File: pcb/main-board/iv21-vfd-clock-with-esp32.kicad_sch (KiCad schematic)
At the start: 24 parts, among them J1 Conn_02x10_Odd_Even, J2 4328, P1 USB_C_Plug_USB2.0, SW1 SW_SPST, SW2 SW_SPST, U1 MAX6921AQI_, U2 MOUDLE-SEEEDUINO-XIAO-ESP32C3, U3 AP3012, U4 S-1167B24

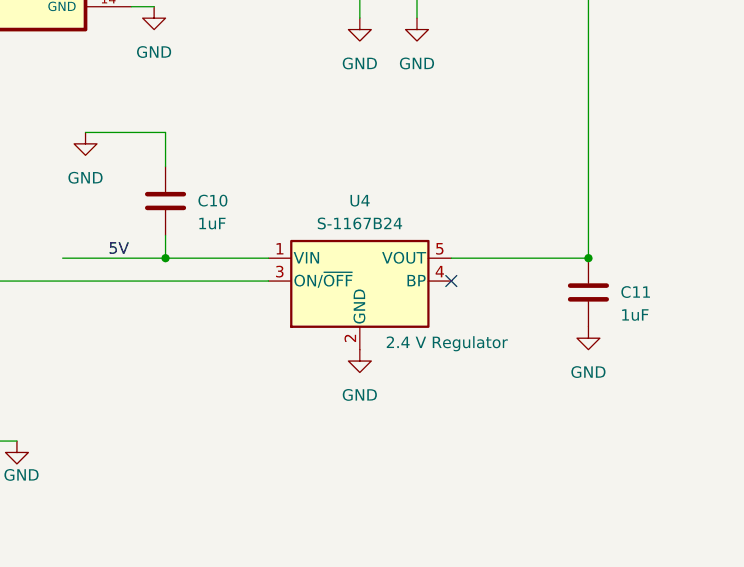
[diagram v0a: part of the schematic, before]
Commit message: Add voltage regulator schematic symbol from dad.
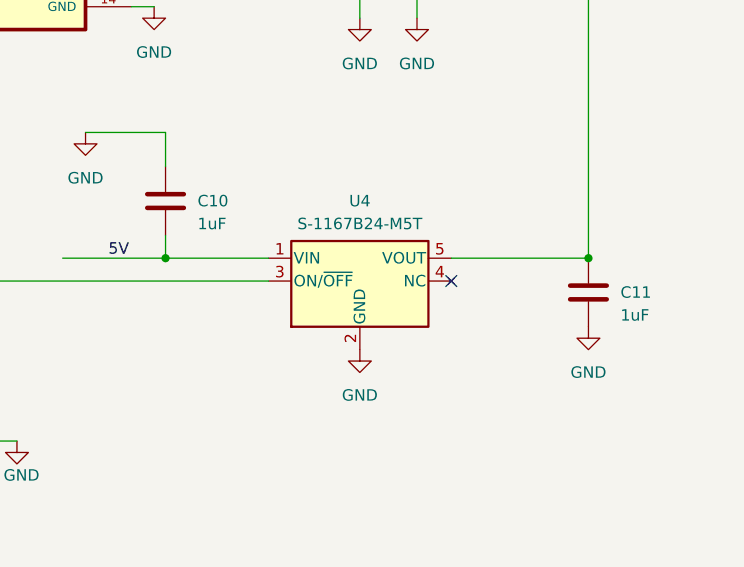
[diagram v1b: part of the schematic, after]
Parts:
- removed U4: S-1167B24, Package_TO_SOT_SMD:SOT-23-5, symbol Regulator_Linear:LP2985-1.8
- added U4: S-1167B24-M5T, Package_TO_SOT_SMD:SOT-23-5, symbol S-1167B24-M5T:LP2985-3.0
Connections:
- net 5V: now also U4.1 (VIN)
- net GND: now also U4.2 (GND)
- net at C11.1, J1.18 (Pin_18): now also U4.5 (VOUT)
- net at U2.3 (PA10_A2_D2): now also U4.3 (ON/~{OFF})
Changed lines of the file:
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@@
-	)
-	(symbol
-		(lib_id "Regulator_Linear:LP2985-1.8")
-		(at 203.2 135.89 0)
-		(unit 1)
-		(exclude_from_sim no)
-		(in_bom yes)
-		(on_board yes)
-		(dnp no)
-		(property "Reference" "U4"
-			(at 203.2 127 0)
-			(effects
-				(font
-					(size 1.27 1.27)
-				)
-			)
-		)
-		(property "Value" "S-1167B24"
-			(at 203.2 129.54 0)
-			(effects
-				(font
-					(size 1.27 1.27)
-				)
-			)
-		)
-		(property "Footprint" "Package_TO_SOT_SMD:SOT-23-5"
-			(at 203.2 127.635 0)
-			(effects
-				(font
-					(size 1.27 1.27)
-				)
-				(hide yes)
-			)
-		)
-		(property "Datasheet" "https://www.mouser.com/datasheet/2/1490/S1167_E-3431012.pdf"
-			(at 203.2 135.89 0)
-			(effects
-				(font
-					(size 1.27 1.27)
-				)
-				(hide yes)
-			)
-		)
-		(property "Description" "S-1167B24-M5T1U: LDO Voltage Regulators ULTRA LOW CURRENT CONSUMPTION, HIGH RIPPLE REJECTION AND LOW DROPOUT CMOS VOLTAGE REGULATOR"
-			(at 203.2 135.89 0)
-			(effects
-				(font
-					(size 1.27 1.27)
-				)
-				(hide yes)
-			)
-		)
-		(property "URL" "https://www.mouser.com/ProductDetail/ABLIC/S-1167B24-M5T1U?qs=2wMNvWM5ZX5qdX7pUf9HBw%3D%3D"
-			(at 203.2 135.89 0)
-			(effects
-				(font
-					(size 1.27 1.27)
-				)
-				(hide yes)
-			)
-		)
-		(property "Label" "2.4 V Regulator"
-			(at 212.852 142.748 0)
-			(effects
-				(font
-					(size 1.27 1.27)
-				)
-			)
-		)
-		(pin "4"
-		)
-		(pin "1"
-		)
-		(pin "3"
-		)
-		(pin "2"
-		)
-		(pin "5"
-		)
-		(instances
-			(project ""
-				(path "/f4ccf12f-2c39-4319-adc8-75ef731d1807"
-					(reference "U4")
-					(unit 1)
-				)
-			)
-		)
 	)
 	(symbol
@@
 					(unit 1)
 				)
+			)
+		)
+	)
+	(symbol
+		(lib_id "S-1167B24-M5T:LP2985-3.0")
+		(at 203.2 135.89 0)
+		(unit 1)
+		(exclude_from_sim no)
+		(in_bom yes)
+		(on_board yes)
+		(dnp no)
+		(fields_autoplaced yes)
+		(property "Reference" "U4"
+			(at 203.2 127 0)
+			(effects
+				(font
+					(size 1.27 1.27)
+				)
+			)
+		)
+		(property "Value" "S-1167B24-M5T"
+			(at 203.2 129.54 0)
+			(effects
+				(font
+					(size 1.27 1.27)
+				)
+			)
+		)
+		(property "Footprint" "Package_TO_SOT_SMD:SOT-23-5"
+			(at 203.2 127.635 0)
+			(effects
+				(font
+					(size 1.27 1.27)
+				)
+				(hide yes)
+			)
+		)
+		(property "Datasheet" "http://www.ti.com/lit/ds/symlink/lp2985.pdf"
+			(at 203.2 135.89 0)
+			(effects
+				(font
+					(size 1.27 1.27)
+				)
+				(hide yes)
+			)
+		)
+		(property "Description" "150mA 16V Low-noise Low-dropout Regulator With Shutdown, 3.0V output voltage, SOT-23-5"
+			(at 203.2 135.89 0)
+			(effects
+				(font
+					(size 1.27 1.27)
+				)
+				(hide yes)
+			)
+		)
+		(pin "1"
+		)
+		(pin "4"
+		)
+		(pin "2"
+		)
+		(pin "3"
+		)
+		(pin "5"
+		)
+		(instances
+			(project ""
+				(path "/f4ccf12f-2c39-4319-adc8-75ef731d1807"
+					(reference "U4")
+					(unit 1)
+				)

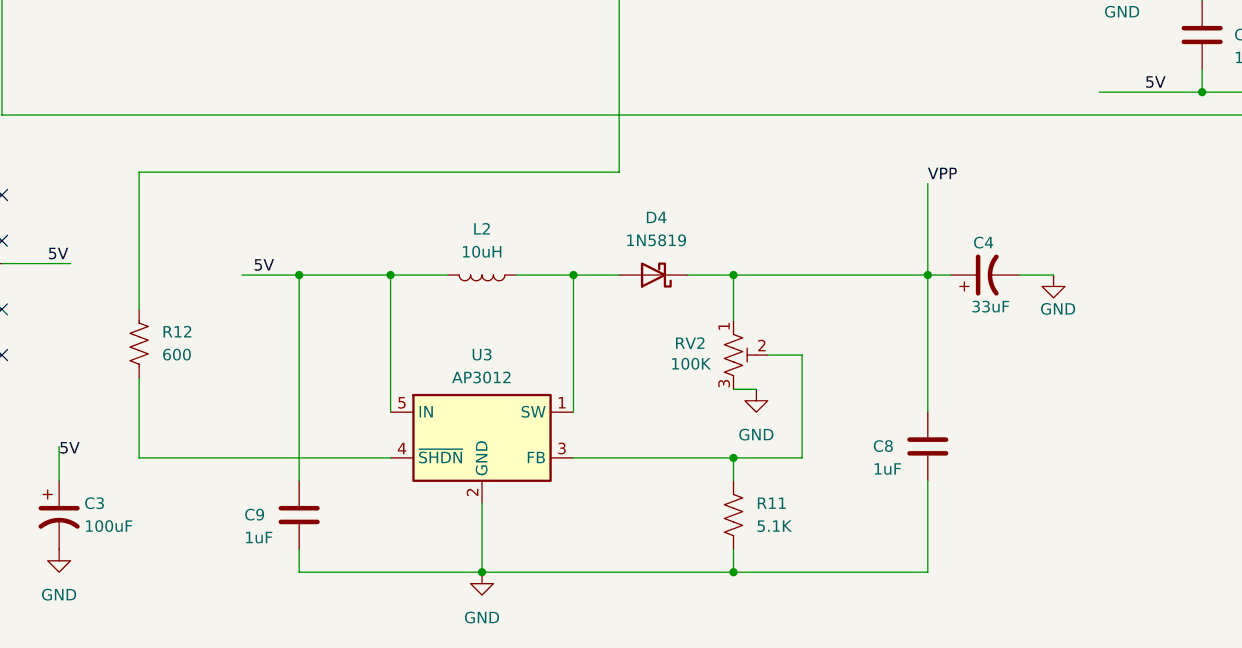
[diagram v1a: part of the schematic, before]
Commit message: Schematic updates for VPP.
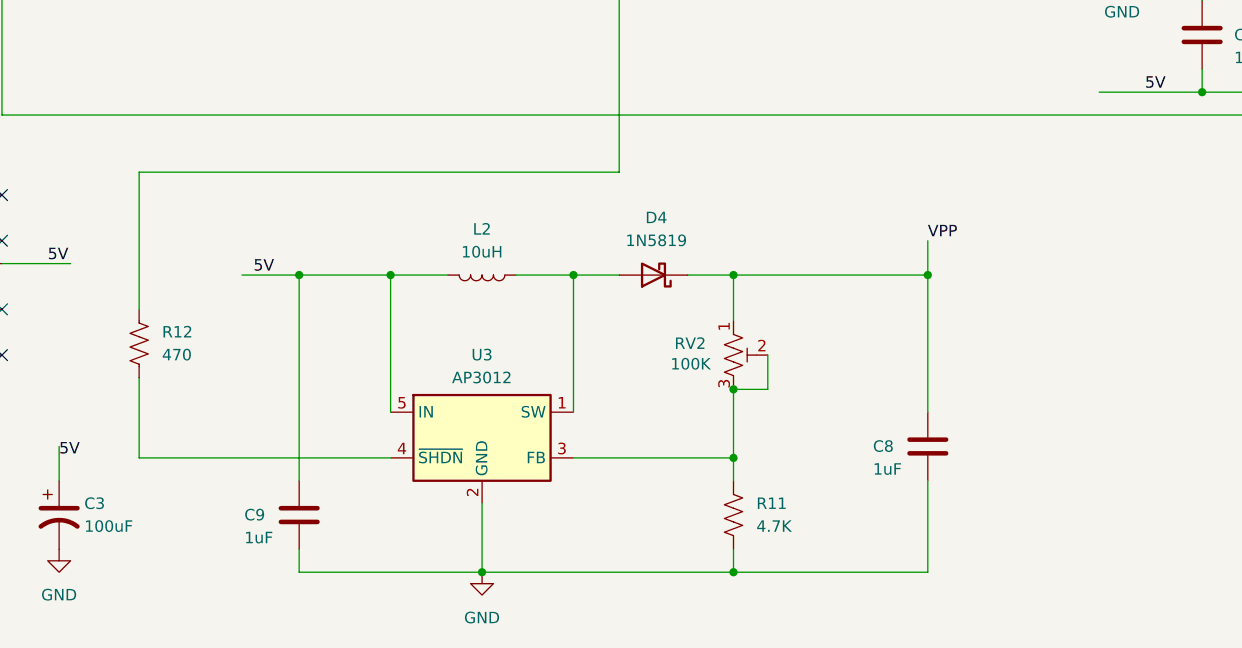
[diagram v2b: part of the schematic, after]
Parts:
- removed C4: 33uF, Capacitor_SMD:CP_Elec_8x10.5, symbol Device:C_Polarized_US
- R11: value 5.1K -> 4.7K
- R12: value 600 -> 470
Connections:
- net GND: no longer RV2.3
- net at R11.1, RV2.2, U3.3 (FB): now also RV2.3

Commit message: - Widen width of power traces. (Need to reroute one of the voltage regulators, still) - Update voltage regulator datasheet and product URL.
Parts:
- U4: Product URL (none) -> https://www.mouser.com/ProductDetail/628-S-1167B24-M5T1U
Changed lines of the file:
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@@
 			)
 		)
-		(property "Datasheet" "http://www.ti.com/lit/ds/symlink/lp2985.pdf"
+		(property "Datasheet" "https://www.mouser.com/datasheet/2/1490/S1167_E-3431012.pdf"
 			(at 203.2 135.89 0)
 			(effects
@@
 			(at 203.2 135.89 0)
 			(effects
+				(font
+					(size 1.27 1.27)
+				)
+				(hide yes)
+			)
+		)
+		(property "Product URL" "https://www.mouser.com/ProductDetail/628-S-1167B24-M5T1U"
+			(at 203.2 135.89 0)
+			(effects

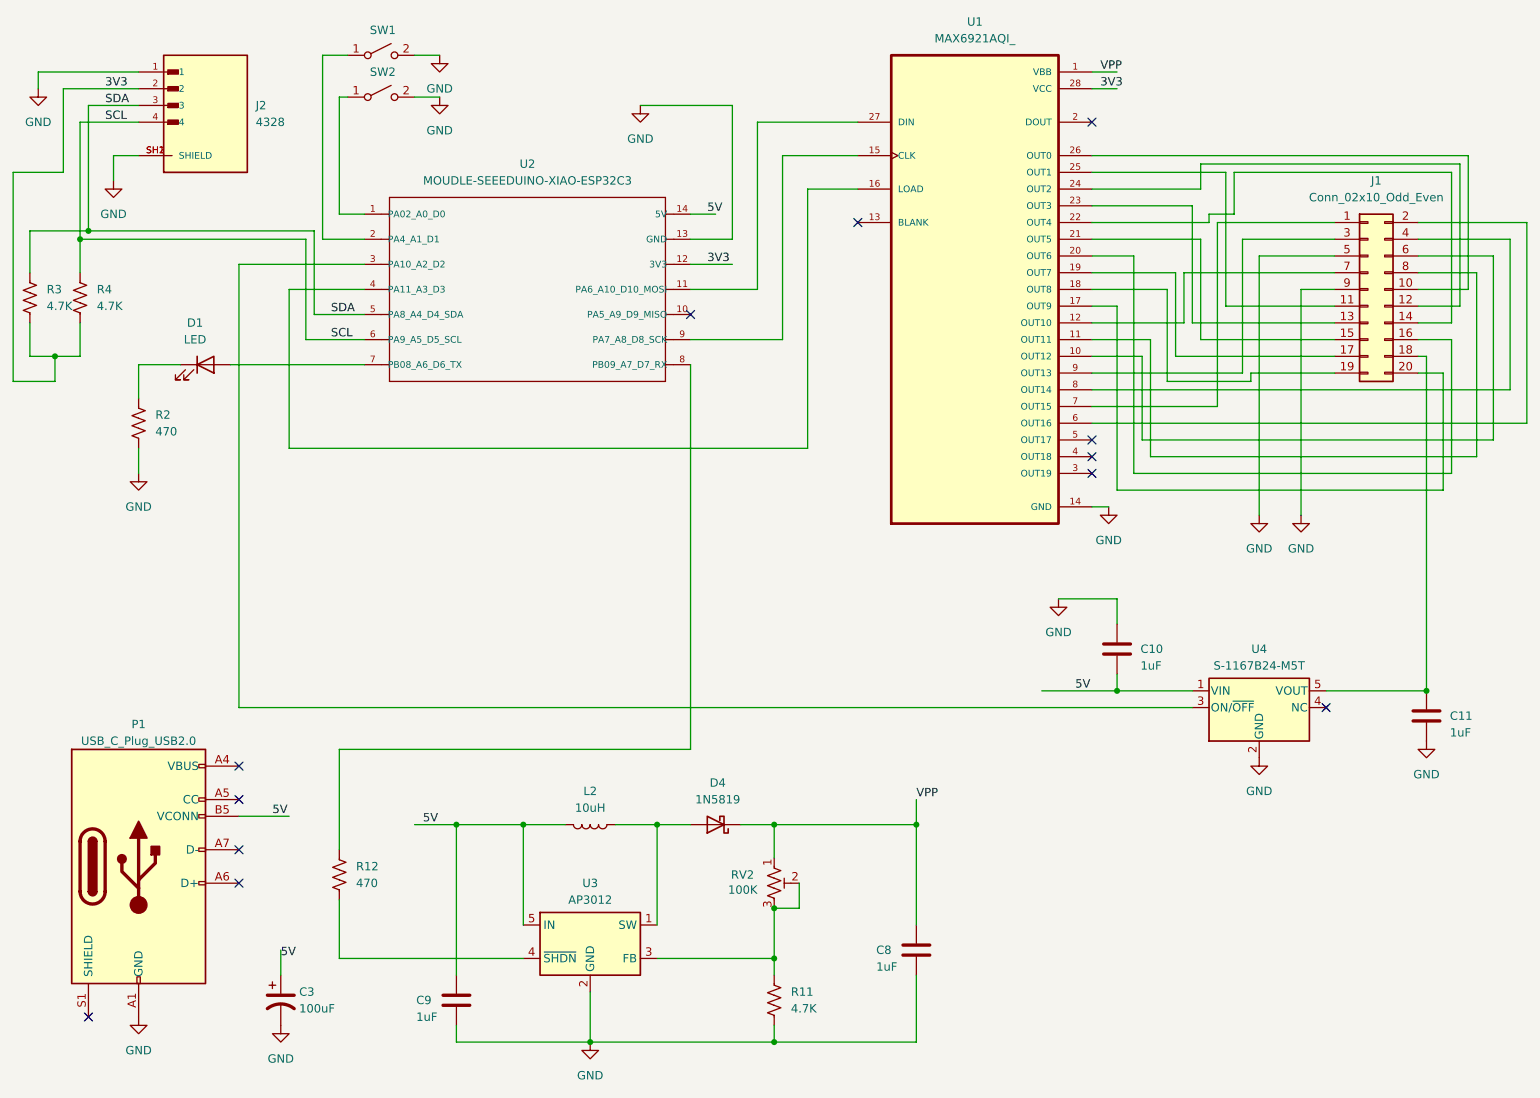
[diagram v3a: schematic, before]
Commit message: - Update power traces - Add in-series resistor with VPP voltage divider trim pot.
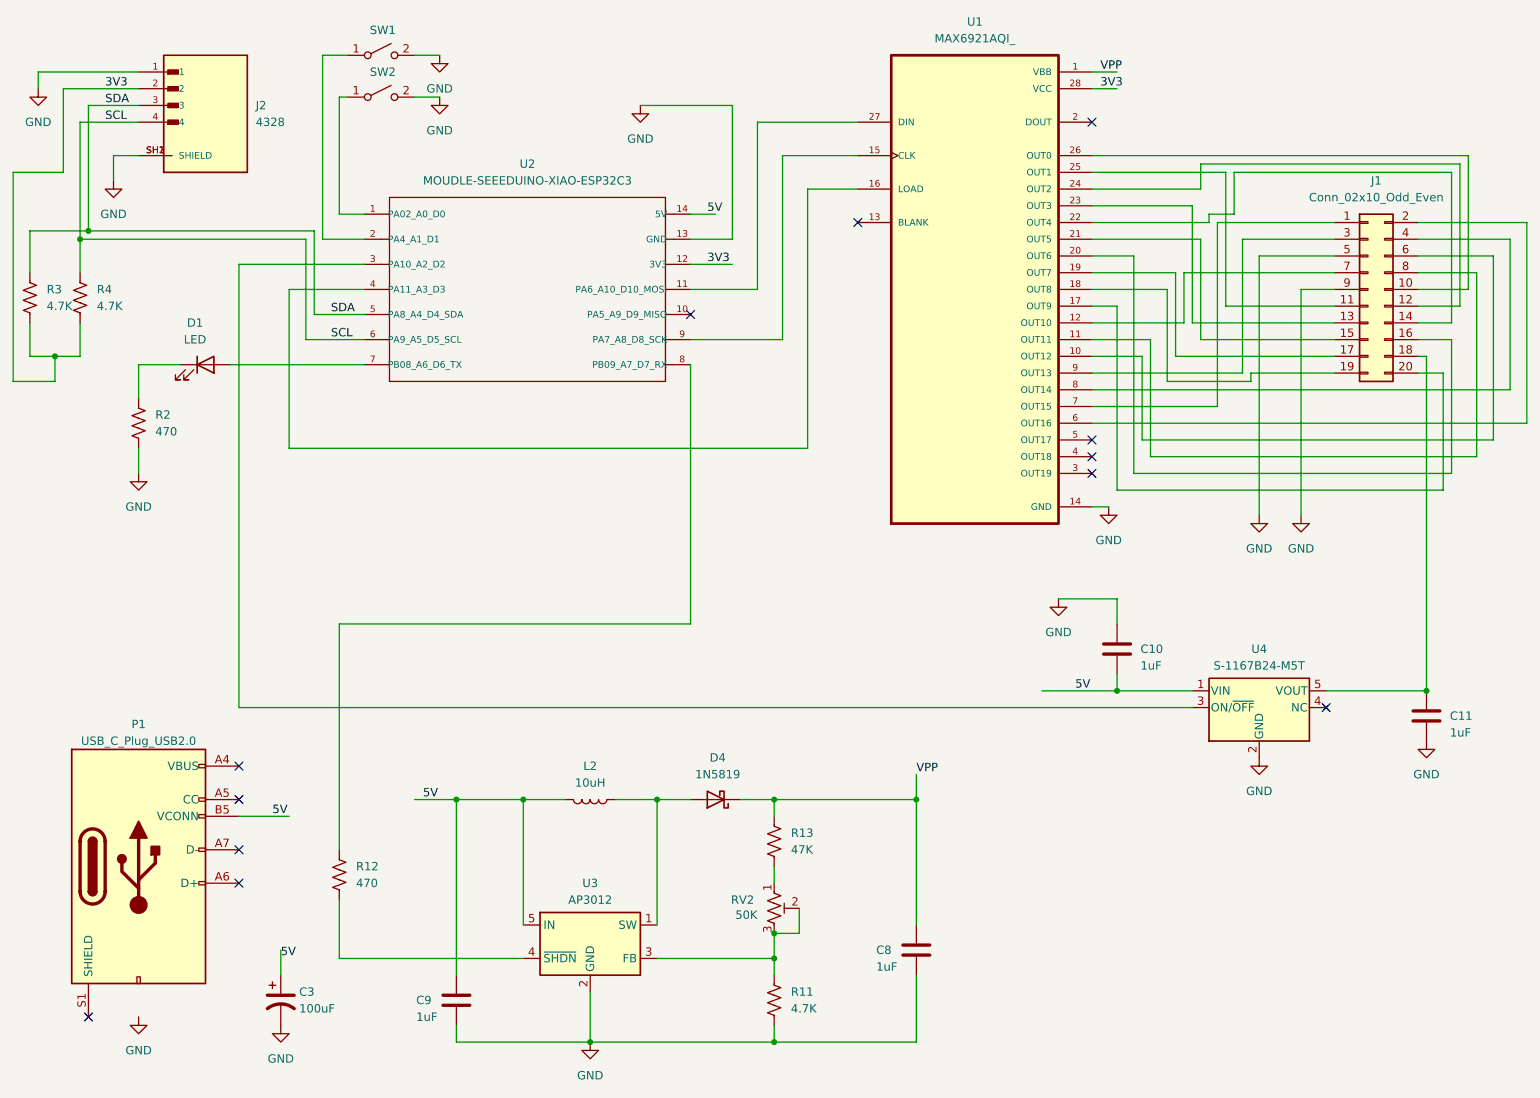
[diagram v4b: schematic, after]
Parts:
- added R13: 47K, Resistor_SMD:R_0805_2012Metric_Pad1.20x1.40mm_HandSolder, symbol Device:R_US
- RV2: value 100K -> 50K
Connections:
- net GND: no longer P1.A1 (GND), P1.B1 (GND)
- net VPP: now also R13.1; no longer RV2.1
- net at P1.A4 (VBUS), P1.B4 (VBUS): no longer P1.A9 (VBUS), P1.B9 (VBUS)
- new net: R13.2, RV2.1
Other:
- moved on the sheet: D4, L2, RV2

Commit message: change resistor value.
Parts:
- R13: value 47K -> 75K
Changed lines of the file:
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@@
 			)
 		)
-		(property "Value" "47K"
+		(property "Value" "75K"
 			(at 132.08 157.4799 0)
 			(effects

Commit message: Add 470R resistor to S-1167B24 on/off pin
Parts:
- added R14: 470, Resistor_SMD:R_0805_2012Metric_Pad1.20x1.40mm_HandSolder, symbol Device:R_US
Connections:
- net at U4.3 (ON/~{OFF}): now also R14.1; no longer U2.3 (PA10_A2_D2)
- new net: R14.2, U2.3 (PA10_A2_D2)
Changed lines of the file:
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@@
-	(wire
-		(pts
-			(xy 48.26 135.89) (xy 193.04 135.89)
-		)
-		(stroke
-			(width 0)
-			(type default)
-		)
-	)
 	(wire
 		(pts
@@
 	(wire
 		(pts
+			(xy 146.05 135.89) (xy 193.04 135.89)
+		)
+		(stroke
+			(width 0)
+			(type default)
+		)
+	)
+	(wire
+		(pts
 			(xy 24.13 82.55) (xy 20.32 82.55)
 		)
@@
 		(pts
 			(xy 177.8 54.61) (xy 198.12 54.61)
+		)
+		(stroke
+			(width 0)
+			(type default)
+		)
+	)
+	(wire
+		(pts
+			(xy 48.26 135.89) (xy 138.43 135.89)
 		)
 		(stroke
@@
 					(unit 1)
 				)
+			)
+		)
+	)
+	(symbol
+		(lib_id "Device:R_US")
+		(at 142.24 135.89 270)
+		(unit 1)
+		(exclude_from_sim no)
+		(in_bom yes)
+		(on_board yes)
+		(dnp no)
+		(fields_autoplaced yes)
+		(property "Reference" "R14"
+			(at 142.24 129.54 90)
+			(effects
+				(font
+					(size 1.27 1.27)
+				)
+			)
+		)
+		(property "Value" "470"
+			(at 142.24 132.08 90)
+			(effects
+				(font
+					(size 1.27 1.27)
+				)
+			)
+		)
+		(property "Footprint" "Resistor_SMD:R_0805_2012Metric_Pad1.20x1.40mm_HandSolder"
+			(at 141.986 136.906 90)
+			(effects
+				(font
+					(size 1.27 1.27)
+				)
+				(hide yes)
+			)
+		)
+		(property "Datasheet" "~"
+			(at 142.24 135.89 0)
+			(effects
+				(font
+					(size 1.27 1.27)
+				)
+				(hide yes)
+			)
+		)
+		(property "Description" "Resistor, US symbol"
+			(at 142.24 135.89 0)
+			(effects
+				(font
+					(size 1.27 1.27)
+				)
+				(hide yes)
+			)
+		)
+		(pin "1"
+		)
+		(pin "2"
+		)
+		(instances
+			(project "iv21-vfd-clock-with-esp32"
+				(path "/f4ccf12f-2c39-4319-adc8-75ef731d1807"
+					(reference "R14")
+					(unit 1)
+				)
